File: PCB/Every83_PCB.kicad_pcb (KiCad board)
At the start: 4 copper layers, 329.9 x 120.9 mm, 287 parts, among them J1 781710004, J2 Conn_01x08_Socket, J3 SM03B-SRSS-TB, J4 SM03B-SRSS-TB, J5 Conn_01x08_Socket, Q3 DMG2305, SW101 KMR2, SW102 KMR2, U1 Core52840, U2 AP2112(3.3V)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

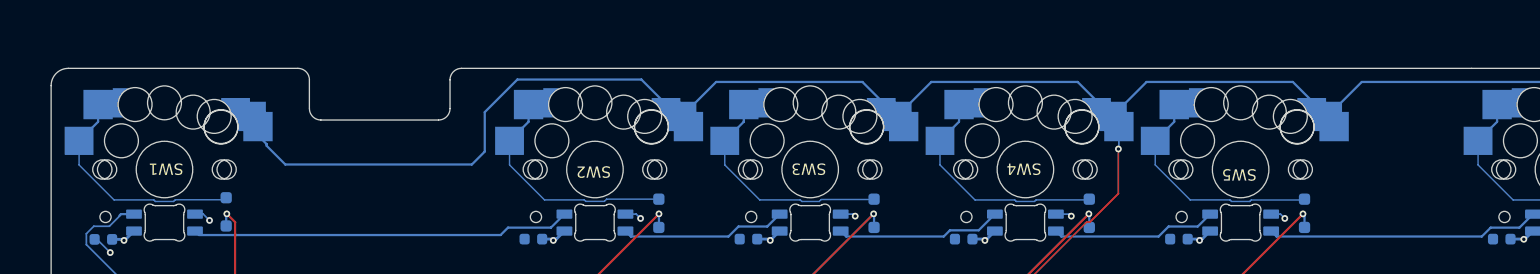
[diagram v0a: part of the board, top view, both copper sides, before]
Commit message: add power switch
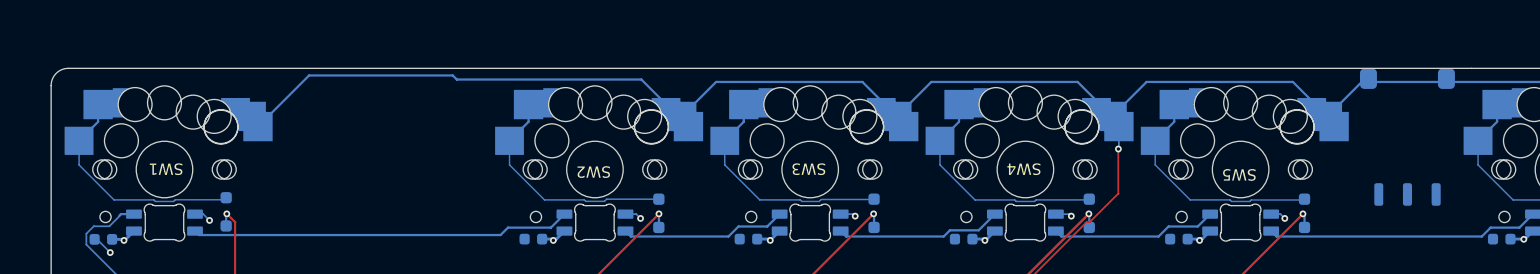
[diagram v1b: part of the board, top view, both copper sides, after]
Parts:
- added SW84: SW_SPDT, JohnDeereLibrary:ET01M3D1SA1BE, B.Cu at (164.5, 40.3)
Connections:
- X1 pad 2: VBAT -> Net-(SW84-C)
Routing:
- net Row0: track 478.4 -> 473.3 mm
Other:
- outline, holes or cut-outs redrawn

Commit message: smol changes
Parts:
- removed SW84: SW_SPDT, JohnDeereLibrary:ET01M3D1SA1BE
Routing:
- net Row0: track 473.3 -> 508.3 mm, vias 2 -> 4
- net Net-(SW5B-DO): track 24.2 -> 28.7 mm
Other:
- outline, holes or cut-outs redrawn

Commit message: small changes to UX for charging
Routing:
- net 12: track 194.2 -> 1.49 mm
- net 13: track 192.0 -> 1.13 mm
- net 8: track 50.4 -> 1.13 mm
- net 9: track 50.3 -> 1.13 mm
- net 10: track 50.0 -> 1.13 mm
- net 14: track 49.7 -> 1.33 mm
- net 11: track 48.8 -> 1.30 mm
- net 15: track 40.6 -> 1.02 mm
- net 16: track 10.6 -> 1.70 mm

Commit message: Change the layout of the power section
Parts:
- removed D103: LED, Diode_SMD:D_0805_2012Metric_Pad1.15x1.40mm_HandSolder
- removed R3: 1K, Resistor_SMD:R_0603_1608Metric
- removed X1: JST SM02B-SRSS-TB(LF)(SN), Connector_JST:JST_SH_SM02B-SRSS-TB_1x02-1MP_P1.00mm_Horizontal
- added J1: 781710004, footprints:CON_781710004, F.Cu at (280.2, 193.3)
- added J8: Conn_01x04_Pin, Connector_JST:JST_SH_SM04B-SRSS-TB_1x04-1MP_P1.00mm_Horizontal, B.Cu at (152.9, 59.9)
- added R10: 100k, Resistor_SMD:R_0603_1608Metric, F.Cu at (285.2, 203.2)
- added R9: 100k, Resistor_SMD:R_0603_1608Metric, F.Cu at (285.2, 200.7)
- J2, J5: footprint Connector_PinHeader_2.54mm:PinHeader_1x08_P2.54mm_Vertical -> Connector_PinHeader_1.00mm:PinHeader_1x08_P1.00mm_Vertical
- moved C3 150.8 mm to (156.4, 4.34)
- moved C6 150.8 mm to (155.2, -4.83)
- moved C7 150.8 mm to (155.5, -0.46)
- moved C8 150.8 mm to (158.9, 1.81)
- moved D101 150.8 mm to (157.9, -4.14)
- moved Q3 150.8 mm to (162.4, -4.70)
- moved R7 150.8 mm to (165.9, -2.87)
- moved R8 150.8 mm to (162.4, -1.47)
- moved U2 150.8 mm to (162.4, 1.81)
- moved R12 150.8 mm to (179.7, 5.38)
- moved R9 150.8 mm to (175.7, 5.38)
- moved R4 108.8 mm to (138.7, 59.7), turned to -90 degrees
- moved U3 107.6 mm to (142.7, 59.9), turned to 180 degrees
- moved C9 104.7 mm to (147.3, 59.9), turned to 90 degrees
- moved U1 47.5 mm to (195.6, 141.8), turned to -90 degrees
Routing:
- net Row0: track 508.3 -> 0.00 mm, vias 4 -> 0
- net Col15: track 469.3 -> 0.00 mm, vias 4 -> 0
- net Col14: track 448.2 -> 0.00 mm, vias 6 -> 0
- net Row1: track 447.6 -> 0.00 mm, vias 2 -> 0
- net Col13: track 431.5 -> 0.00 mm, vias 7 -> 0
- net Row2: track 412.4 -> 0.00 mm, vias 2 -> 0
- net Col12: track 402.6 -> 0.00 mm, vias 5 -> 0
- net Col10: track 400.2 -> 0.00 mm, vias 7 -> 0
- net Col9: track 378.1 -> 0.00 mm, vias 7 -> 0
- net Net-(SW60B-DO): track 364.1 -> 0.00 mm, vias 2 -> 0
- net Net-(SW73B-DO): track 372.4 -> 12.6 mm, vias 2 -> 0
- net Col11: track 352.5 -> 0.00 mm, vias 5 -> 0
- net Row4: track 346.2 -> 0.00 mm, vias 4 -> 0
- net Row5: track 345.5 -> 0.00 mm, vias 6 -> 0
- net Net-(SW15B-DO): track 340.0 -> 0.00 mm
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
